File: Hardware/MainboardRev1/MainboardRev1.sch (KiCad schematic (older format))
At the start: 14 parts

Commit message: Added some more circuitry to power schematic
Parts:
- removed R?: 32.4k, symbol R
- removed R?: 11.5k, symbol R
- added C? (x4): 10uF, symbol C
- added D? (x2): D_Schottky, symbol D_Schottky
- added D?: 3.3V, symbol ZENER
- added Q?: SSM3J328R, symbol Q_PMOS_GSD
- added Q?: NTR4003, symbol Q_NMOS_GSD
- added R? (x2): 10k, symbol R
- added SW?: SPDT, symbol Switch_SPDT_x2
- added U?: LTC3605, symbol LTC3605
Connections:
- net labels added: Backup_Batt, Battery_Power, Main_Batt
- wire segments 20 -> 57
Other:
- moved on the sheet: Q?, R?

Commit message: Schematic Finished. Needs Review & Final Touches. Beginning Footprints...:
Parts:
- removed C? (x2): 10uF, symbol C
- removed D? (x2): D_Schottky, symbol D_Schottky
- removed D?: 3.3V, symbol ZENER
- removed Q?: SSM3J328R, symbol Q_PMOS_GSD
- removed Q?: NTR4003, symbol Q_NMOS_GSD
- removed R? (x2): 10k, symbol R
- removed SW?: SPDT, symbol Switch_SPDT_x2
- added C1, C10, C11, C12, C13: 47uF, symbol C
- added C14, C19: 1uF, symbol C
- added C15, C16, C17, C18, C20, C21: 4.7uF, symbol C
- added C4, C6, C7: 0.1uF, symbol C
- added C5: .01uF, symbol C
- added C8: 10pF, symbol C
- added C9: 220pF, symbol C
- added D1, D2: 5.6V, symbol ZENERsmall
- added D10: Red, symbol LED
- added D3: CMDSH2-3, symbol D_Schottky
- added D4: SL42-E3/57T, symbol D_Schottky
- added D5: +3.3V_Zener, symbol ZENER
- added D6, D7, D8, D9: Green, symbol LED
- added L1: RLF7030T-2R2M5R4 [2.2uH], symbol INDUCTOR_SMALL
- added Q1, Q10, Q2, Q8: SSM3J328R, symbol Q_PMOS_GSD
- added Q11, Q12, Q13, Q7, Q9: NTR4003, symbol Q_NMOS_GSD
- added R1, R2, R34: 100k, symbol R
- added R14, R9: 500, symbol R
- added R15: 16k, symbol R
- added R16, R21: 10K, symbol R
- added R17: 118k, symbol R
- added R18, R20, R23, R4: 10k, symbol R
- added R19: 2k, symbol R
- added R22: 12k, symbol R
- added R24, R31, R5: 10, symbol R
- added R25, R28: 10m, symbol R
- added R26, R29, R32, R37: 1M, symbol R
- added R27, R30, R33, R38: 11.5k, symbol R
- added R3: 140k, symbol R
- added R35, R36: 25m, symbol R
- added R39, R40, R41, R42, R43: R, symbol R
- added R7: 200k, symbol R
- added SW1: SW_DPDT_x2, symbol SW_DPDT_x2
- added U1: LT6703-3, symbol LT6703-3
- added U3, U4: LTC4358, symbol LTC4358
- added U5: LDL1117S50R, SOT-223, symbol LD1117S12CTR
- added U6, U8: LDL1117S33R, SOT-223, symbol LD1117S12CTR
- added U7, U9: LTC2992, symbol LTC2992
- C2, C3: renamed from C?; value 10uF -> 47uF
- gave numbers to parts that had none: 13
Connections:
- net labels added: +3.3V, +3.3V_DIVIDER, +3.3V_MSMT, +3.3V_STARTUP, +5V, +5V_DIVIDER, +5V_MSMT, +6.5V, +6.5V_DIVIDER, +6.5V_MSMT, BACKUP_BATT, BATTERY_DIVIDER, BATTERY_PWR, BATTERY_PWR_MSMT, CONTROL_1, CONTROL_2, DATA_READY, DATA_READY_1, LDO_FEED, MAIN_BATT, SENSORS_SCL, SENSORS_SDA, STARTUP_BATT, SVIN
- net labels removed: Backup_3.3, Backup_Batt, Battery_Power, Main_Batt
- wire segments 57 -> 220
- no-connect marks 0 -> 12
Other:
- note added: "3S LiPo to 6.5V/5A with Switching Regulator"
- note added: "6.5V Failure Detection and Switchover"
- note added: "6.5V to 5V and\n3.3V Linear Regulators"
- note added: "Current and Voltage Measurement of All Four Voltage Rails"
- note added: "Digital Control of\nMain & Backup\nBatteries"
- note added: "I2C Address 0x6E"
- note added: "I2C Address 0x6F"
- note added: "Ideal Diode "OR""
- note added: "Note: Make sure to use at least half-watt resistors for current sense"
- note added: "Note: There are two methods for \nstartup voltage here. Do not\nplace the zener diode and resistor\nunless the LDO fails to work"
- note added: "Power Indicator LEDs"
- note added: "Reverse Polarity\nProtection &\nFiltering"
- note added: "Startup Voltage Regulation \nfrom Backup Battery"
- moved on the sheet: C2, C3, J1, J2, Q3, Q4, Q5, Q6, R10, R11, R12, R13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

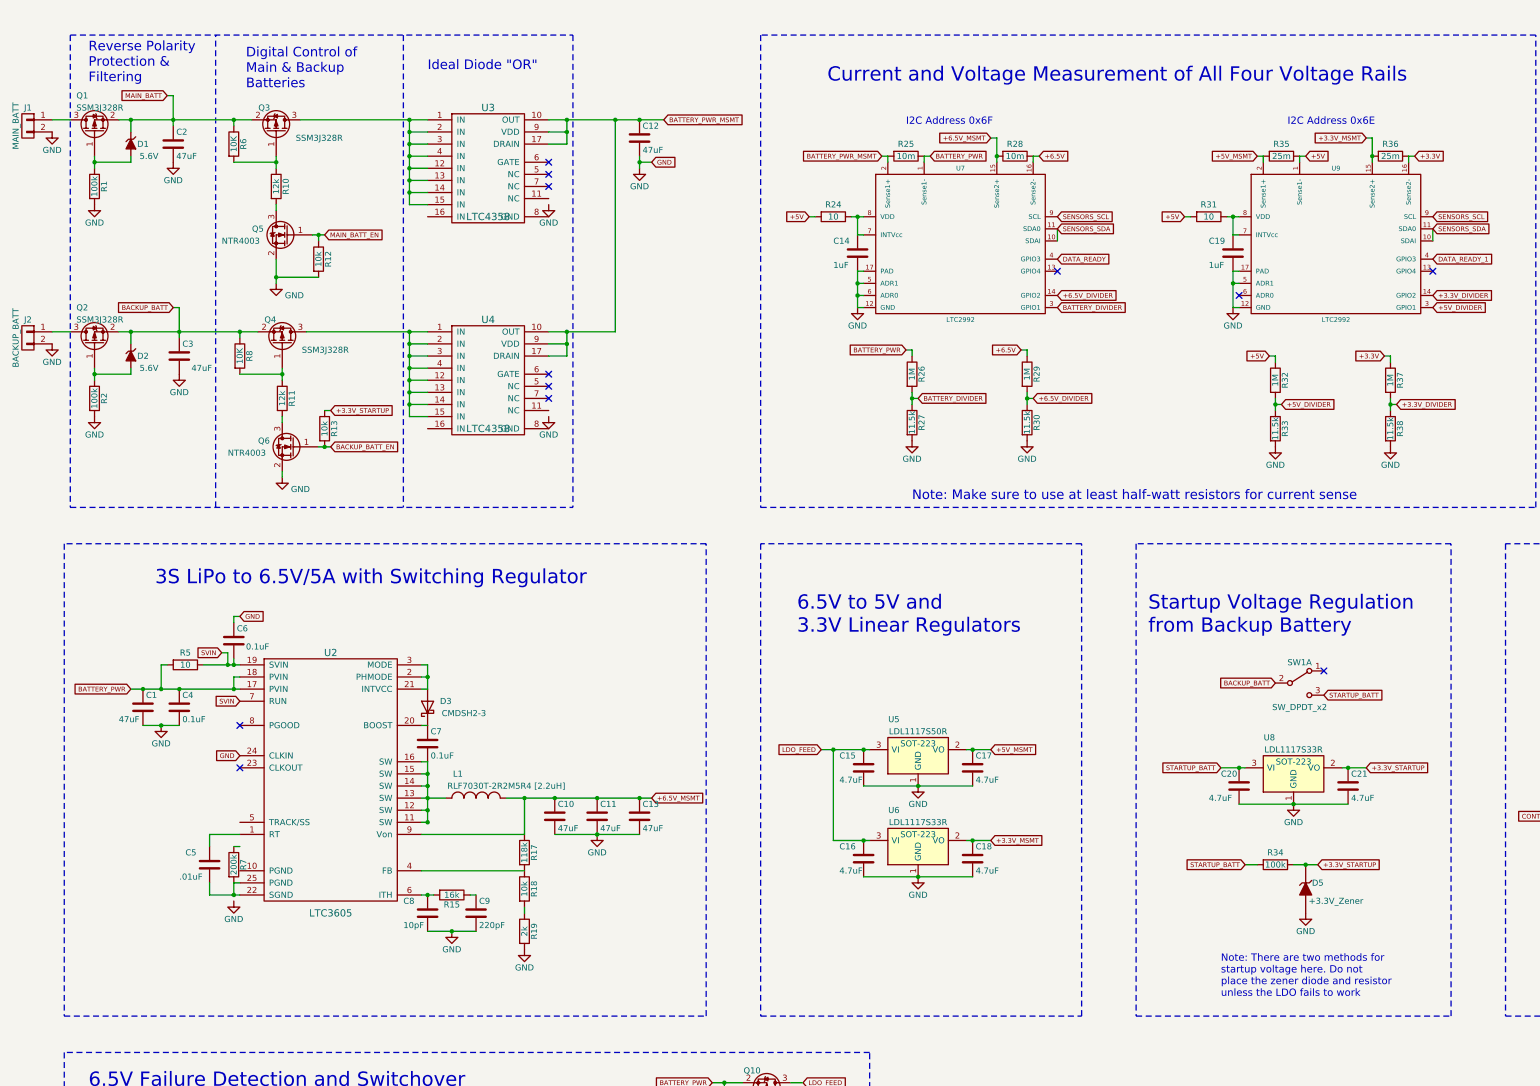
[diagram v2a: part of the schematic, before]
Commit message: Small changes to schematic: Added voltage dividers for analog inputs, small net changes. Added footprints for each part
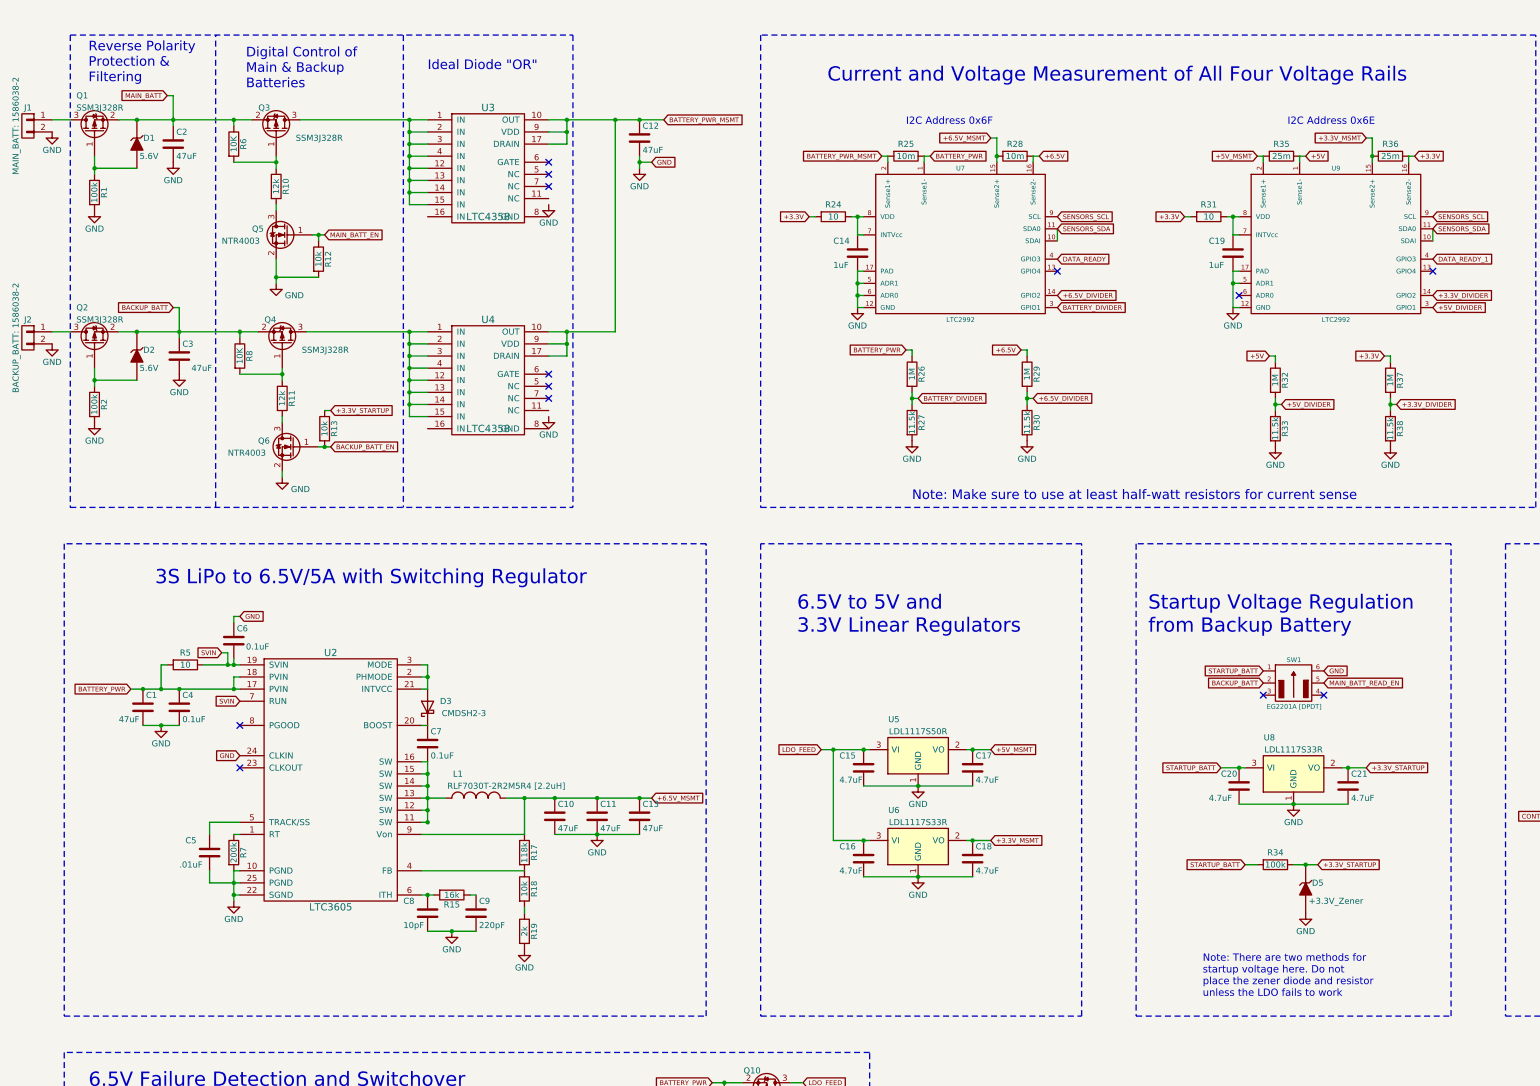
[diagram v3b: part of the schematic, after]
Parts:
- removed D1, D2: 5.6V, symbol ZENERsmall
- removed SW1: SW_DPDT_x2, symbol SW_DPDT_x2
- added D1, D2: 5.6V, Dans_Parts:SOD-323_Diode, symbol ZENER
- added SW1: EG2201A [DPDT], Dans_Parts:SW_DPDT_30V_200mA_EG2201A, symbol SWITCH_DPDT
- C1, C10, C11, C12, C13, C2, C3: footprint (none) -> Capacitors_SMD:C_1210_HandSoldering
- C14, C15, C16, C17, C18, C19, C20, C21, C4, C5, C6, C7, C8, C9: footprint (none) -> Capacitors_SMD:C_0603_HandSoldering
- D10, D6, D7, D8, D9: footprint (none) -> LEDs:LED_0603_HandSoldering
- D3, D5: footprint (none) -> Dans_Parts:SOD-323_Diode
- D4: footprint (none) -> Dans_Parts:DO-214AB_Zener
- J1: value MAIN_BATT -> MAIN_BATT: 1586038-2; footprint (none) -> Dans_Parts:CONN_2POS_VERT_TE_CONN
- J2: value BACKUP_BATT -> BACKUP_BATT: 1586038-2; footprint (none) -> Dans_Parts:CONN_2POS_VERT_TE_CONN
- L1: footprint (none) -> Dans_Parts:IND_RLF7030
- Q1, Q10, Q11, Q12, Q13, Q2, Q3, Q4, Q5, Q6, Q7, Q8, Q9: footprint (none) -> TO_SOT_Packages_SMD:SOT-23
- R1, R10, R11, R12, R13, R14, R15, R16, R17, R18, R19, R2, R20, R21, R22, R23, R24, R26, R27, R29, R3, R30, R31, R32, R33, R34, R37, R38, R39, R4, R40, R41, R42, R43, R5, R6, R7, R8, R9: footprint (none) -> Resistors_SMD:R_0603_HandSoldering
- R25, R28, R35, R36: footprint (none) -> Resistors_SMD:R_0805_HandSoldering
- U1: footprint (none) -> TO_SOT_Packages_SMD:SOT-23-5_HandSoldering
- U2: footprint (none) -> Dans_Parts:QFN25_4x4mm_0.5mm_pitch
- U3, U4: footprint (none) -> Housings_SSOP:TSSOP-16-1EP_4.4x5mm_Pitch0.65mm
- U5, U6, U8: footprint SOT-223 -> TO_SOT_Packages_SMD:SOT-223
- U7, U9: footprint (none) -> Housings_DFN_QFN:DFN-16-1EP_3x4mm_Pitch0.45mm
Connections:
- net +3.3V: now also R24.2, R31.2
- net +5V: no longer R24.2, R31.2
- net BACKUP_BATT: now also D2.1 (K), SW1.2
- net GND: now also C5.2, R7.2, U2.10 (PGND), U2.22 (SGND), U2.25 (PGND), SW1.6
- net MAIN_BATT: now also D1.1 (K)
- net STARTUP_BATT: now also SW1.1
- net at U2.1 (RT): now also R7.1; no longer C5.1
- net at U2.5 (TRACK/SS): now also C5.1
- net at Q1.1 (G), R1.1: now also D1.2 (A)
- net at Q2.1 (G), R2.1: now also D2.2 (A)
- new net MAIN_BATT_READ_EN: SW1.5
- no-connect marks 12 -> 13
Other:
- moved on the sheet: C5, R1, R2, R7

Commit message: Components placed. Needs to be routed.
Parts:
- removed C1: 47uF, Capacitors_SMD:C_1210_HandSoldering, symbol C
- added C14: 47uF, Capacitors_SMD:C_1210_HandSoldering, symbol C
- added J13: EXTRA_5V, Dans_Parts:CONN_2POS_VERT_TE_CONN_LOCK_5-103669-1, symbol CONN_01X02
- added J14: EXTRA_3V3, Dans_Parts:CONN_2POS_VERT_TE_CONN_LOCK_5-103669-1, symbol CONN_01X02
- added MH1, MH2, MH3, MH4: Mounting Hole, Dans_Parts:Mounting_Hole_3.50mm, symbol Mounting_Hole_Eighth_Inch
- C15: renamed from C14; value 1uF -> 0.1uF
- C16: renamed from C15; value 4.7uF -> 47uF; footprint Capacitors_SMD:C_0603_HandSoldering -> Capacitors_SMD:C_1210_HandSoldering
- C17: renamed from C16; value 4.7uF -> 47uF; footprint Capacitors_SMD:C_0603_HandSoldering -> Capacitors_SMD:C_1210_HandSoldering
- C18: renamed from C17; value 4.7uF -> 47uF; footprint Capacitors_SMD:C_0603_HandSoldering -> Capacitors_SMD:C_1210_HandSoldering
- C19: renamed from C18; value 4.7uF -> 47uF; footprint Capacitors_SMD:C_0603_HandSoldering -> Capacitors_SMD:C_1210_HandSoldering
- C20: renamed from C19; value 1uF -> 0.1uF
- C21: renamed from C20; value 4.7uF -> 47uF; footprint Capacitors_SMD:C_0603_HandSoldering -> Capacitors_SMD:C_1210_HandSoldering
- C22: renamed from C21; value 4.7uF -> 47uF; footprint Capacitors_SMD:C_0603_HandSoldering -> Capacitors_SMD:C_1210_HandSoldering
- J1: value MAIN_BATT: 1586038-2 -> BACKUP_BATT: 1586038-2
- J2: value BACKUP_BATT: 1586038-2 -> MAIN_BATT: 1586038-2
- U5, U6, U8: footprint TO_SOT_Packages_SMD:SOT-223 -> Dans_Parts:SOT-223_Tab_Pin_2
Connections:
- net +3.3V: now also R35.1, U9.1 (Sense1-), J14.2 (P2); no longer R36.1, U9.16 (Sense2-)
- net +3.3V_MSMT: now also R35.2, U9.2 (Sense1+); no longer R36.2, U9.15 (Sense2+)
- net +3.3V_STARTUP: now also R12.1; no longer R13.1
- net +5V: now also R36.1, R39.1, R43.1, U9.16 (Sense2-), J13.2 (P2); no longer D10.2 (A), D6.2 (A), R35.1, U9.1 (Sense1-)
- net +5V_MSMT: now also R36.2, U9.15 (Sense2+); no longer R35.2, U9.2 (Sense1+)
- net BACKUP_BATT: now also C2.1, D1.1 (K), Q1.2 (S), Q3.2 (S), R6.1; no longer C3.1, D2.1 (K), Q2.2 (S), Q4.2 (S), R8.1
- net BACKUP_BATT_EN: now also Q5.1 (G), R12.2; no longer Q6.1 (G), R13.2
- net BATTERY_PWR_MSMT: now also C14.1
- net GND: now also R13.2, U3.8 (GND), U4.8 (GND), C14.2, J13.1 (P1), J14.1 (P1), MH1.1, MH2.1, MH3.1, MH4.1; no longer R12.2
- net MAIN_BATT: now also C3.1, D2.1 (K), Q2.2 (S), Q4.2 (S), R8.1; no longer C2.1, D1.1 (K), Q1.2 (S), Q3.2 (S), R6.1
- net MAIN_BATT_EN: now also Q6.1 (G), R13.1; no longer Q5.1 (G), R12.1
- net at Q3.3 (D), U3.1 (IN), U3.12 (IN)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: now also U3.16 (IN)
- net at Q4.3 (D), U4.1 (IN), U4.12 (IN)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: now also U4.16 (IN)
- net at Q12.3 (D): now also D6.1 (K); no longer R39.2
- net at Q13.3 (D): now also D10.1 (K); no longer R43.2
- new net: D6.2 (A), R39.2
- new net: D10.2 (A), R43.2
- no-connect marks 13 -> 15
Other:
- note added: "Extra Power"
- note added: "Mounting Holes"
- moved on the sheet: C12, C4, D10, D6, R12, R13, R39, R43
